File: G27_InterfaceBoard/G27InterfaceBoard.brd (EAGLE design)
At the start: 60 x 60 mm, 32 parts, among them IC1 LMV321M5, IC2 74HC126D, J1 Pedal, J2 Shifter, U1 LMV324

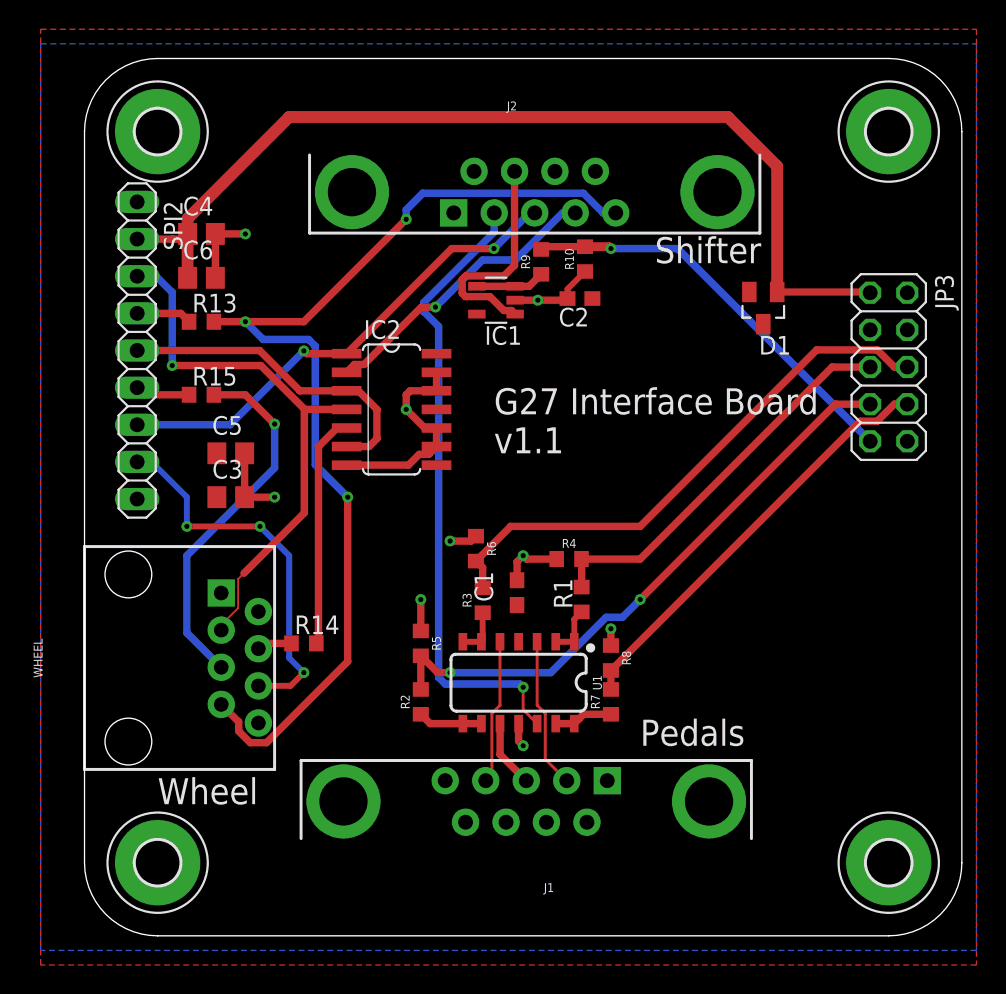
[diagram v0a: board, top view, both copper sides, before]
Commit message: Closer on G27 Interface v1.1:
Use buffer to boost 3.3V signals from STM32 to 5V logic to buy
better noise margin.
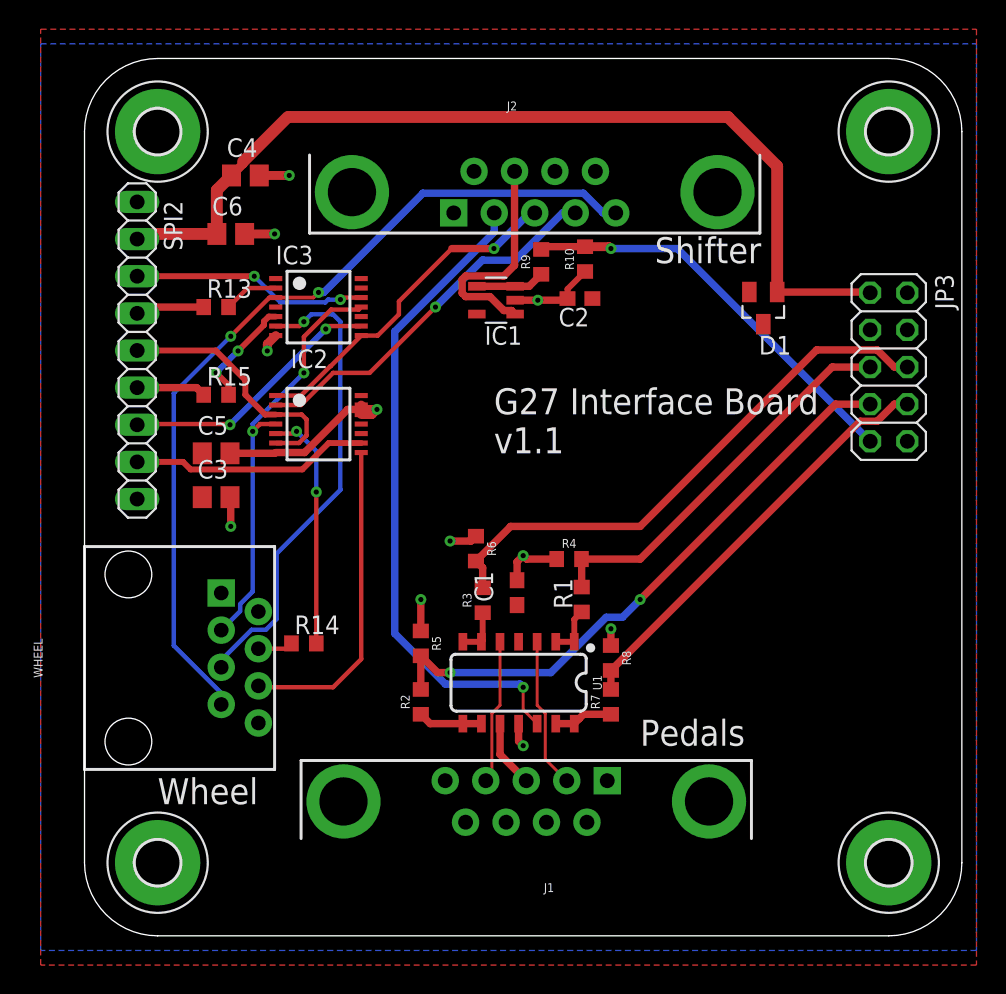
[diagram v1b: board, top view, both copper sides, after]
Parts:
- added IC3: 74AHCT126PW, 74xx-eu:TSSOP14
- IC2: value 74HC126D -> 74AHCT126PW; device 74xx-eu:SO14 -> 74xx-eu:TSSOP14
- R1, R2, R3, R7, R9: value 1.2k -> 1.5k
- moved IC2 5.10 mm to (16.0, -25.0)
- moved C4 5.00 mm to (11.0, -8.00)
- moved C6 3.61 mm to (10.0, -12.0)
- moved R13 1.41 mm to (9.00, -17.0)
- moved C3 1.00 mm to (9.00, -30.0)
- moved C5 1.00 mm to (9.00, -27.0)
- moved R15 1.00 mm to (9.00, -23.0)
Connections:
- new net MOSI_3V3: IC3.5, R15.2
- new net SCK_3V3: IC3.2, R13.2
- new net SHIFT_CS_3V3: IC3.9, SPI2.7
- new net WBTN_CS_3V3: IC3.12, SPI2.3
- new net WLED_LATCH_3V3: IC2.9, SPI2.8
- net GND: now also IC3.7; no longer IC2.10, IC2.9
- net MOSI: now also IC3.6; no longer R15.2
- net SCK: now also IC3.3; no longer R13.2
- net SHIFT_CS: now also IC3.8; no longer SPI2.7
- net VCC: now also IC2.10, IC3.1, IC3.10, IC3.13, IC3.14, IC3.4
- net WBTN_CS: now also IC3.11; no longer SPI2.3
- net WLED_LATCH: now also IC2.8; no longer SPI2.8
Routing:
- net SHIFT_CS_3V3: track 0.00 -> 18.3 mm, vias 0 -> 2
- net WLED_LATCH_3V3: track 0.00 -> 16.3 mm
- net WBTN_CS_3V3: track 0.00 -> 16.2 mm, vias 0 -> 2
- net SCK: track 72.4 -> 59.1 mm, vias 3 -> 2
- net SHIFT_CS: track 33.3 -> 23.4 mm, vias 2 -> 1
- net WBTN_CS: track 38.6 -> 29.0 mm, vias 1 -> 2
- net MOSI_3V3: track 0.00 -> 7.67 mm, vias 0 -> 2
- net MOSI: track 25.1 -> 32.5 mm
- net SHIFT_MISO: track 20.1 -> 25.9 mm
- net +3V3: track 70.9 -> 65.4 mm
- net MISO: track 22.4 -> 17.5 mm
- net GND: track 42.2 -> 37.4 mm, vias 9 -> 11
- net WLED_LATCH: track 26.3 -> 22.0 mm, vias 3 -> 0
- net SCK_3V3: track 0.00 -> 3.76 mm
- net SHIFT_X: track 43.1 -> 44.8 mm
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
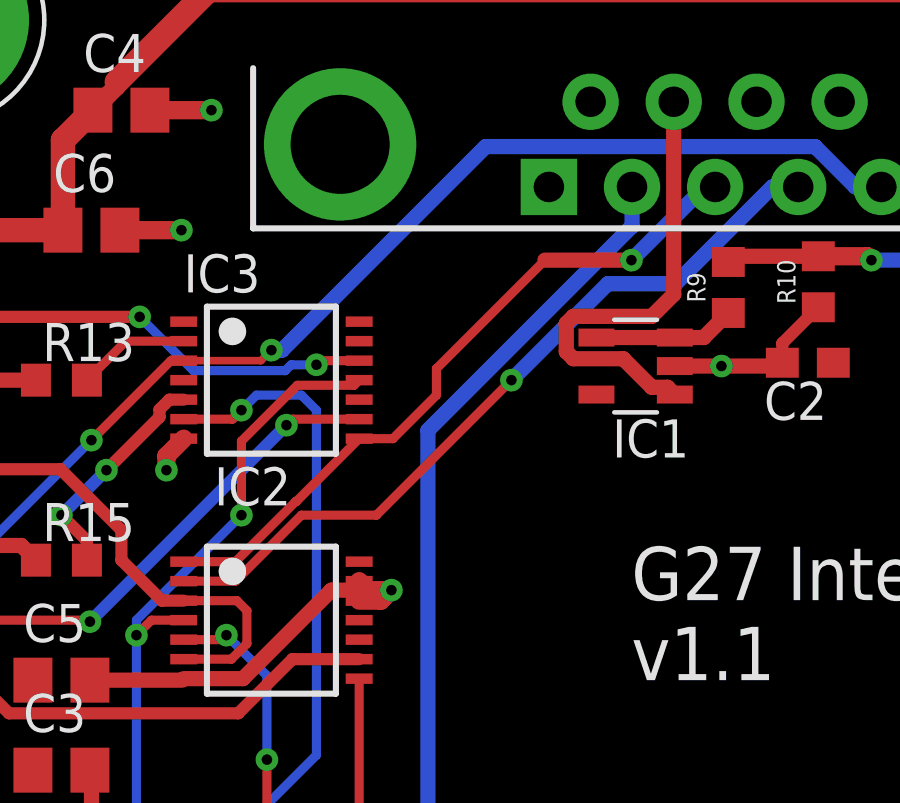
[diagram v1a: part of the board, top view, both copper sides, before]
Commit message: Add additional filter caps.
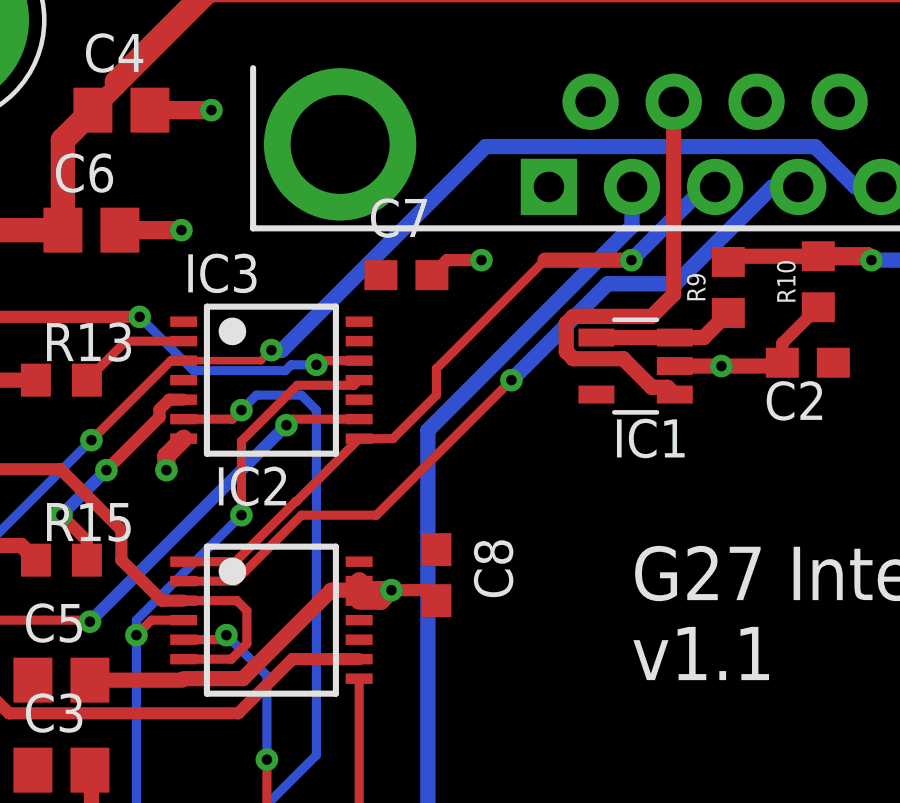
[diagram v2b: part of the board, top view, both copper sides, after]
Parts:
- added C7, C8: 0.1uF, resistor:C0603
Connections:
- net GND: now also C7.2, C8.2
- net VCC: now also C7.1, C8.1
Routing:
- net GND: track 37.4 -> 40.9 mm, vias 11 -> 12
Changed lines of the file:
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@@
 <attribute name="NAME" x="13.075" y="-14.075" size="1.27" layer="25"/>
+</element>
+<element name="C7" library="resistor" library_urn="urn:adsk.eagle:library:348" package="C0603" package3d_urn="urn:adsk.eagle:package:23616/2" value="0.1uF" x="20.5" y="-13.5" smashed="yes">
+<attribute name="NAME" x="19.23" y="-12.23" size="1.27" layer="25"/>
+<attribute name="VALUE" x="19.23" y="-16.04" size="1.27" layer="27"/>
+</element>
+<element name="C8" library="resistor" library_urn="urn:adsk.eagle:library:348" package="C0603" package3d_urn="urn:adsk.eagle:package:23616/2" value="0.1uF" x="21.5" y="-23.5" smashed="yes" rot="R270">
+<attribute name="NAME" x="22.77" y="-22.23" size="1.27" layer="25" rot="R270"/>
+<attribute name="VALUE" x="18.96" y="-22.23" size="1.27" layer="27" rot="R270"/>
 </element>
 </elements>
@@
 <wire x1="10" y1="-30.05" x2="10" y2="-32" width="0.508" layer="1"/>
 <via x="10" y="-32" extent="1-16" drill="0.35"/>
+<contactref element="C7" pad="2"/>
+<contactref element="C8" pad="2"/>
+<wire x1="21.5" y1="-24.35" x2="21.15" y2="-24" width="0.4064" layer="1"/>
+<wire x1="21.15" y1="-24" x2="20" y2="-24" width="0.4064" layer="1"/>
+<wire x1="21.35" y1="-13.5" x2="21.85" y2="-13" width="0.4064" layer="1"/>
+<wire x1="21.85" y1="-13" x2="23" y2="-13" width="0.4064" layer="1"/>
+<via x="23" y="-13" extent="1-16" drill="0.35"/>
 </signal>
 <signal name="SCK">
@@
 <contactref element="IC3" pad="10"/>
 <contactref element="IC3" pad="13"/>
+<contactref element="C7" pad="1"/>
+<contactref element="C8" pad="1"/>
 </signal>
 <signal name="WMISO">

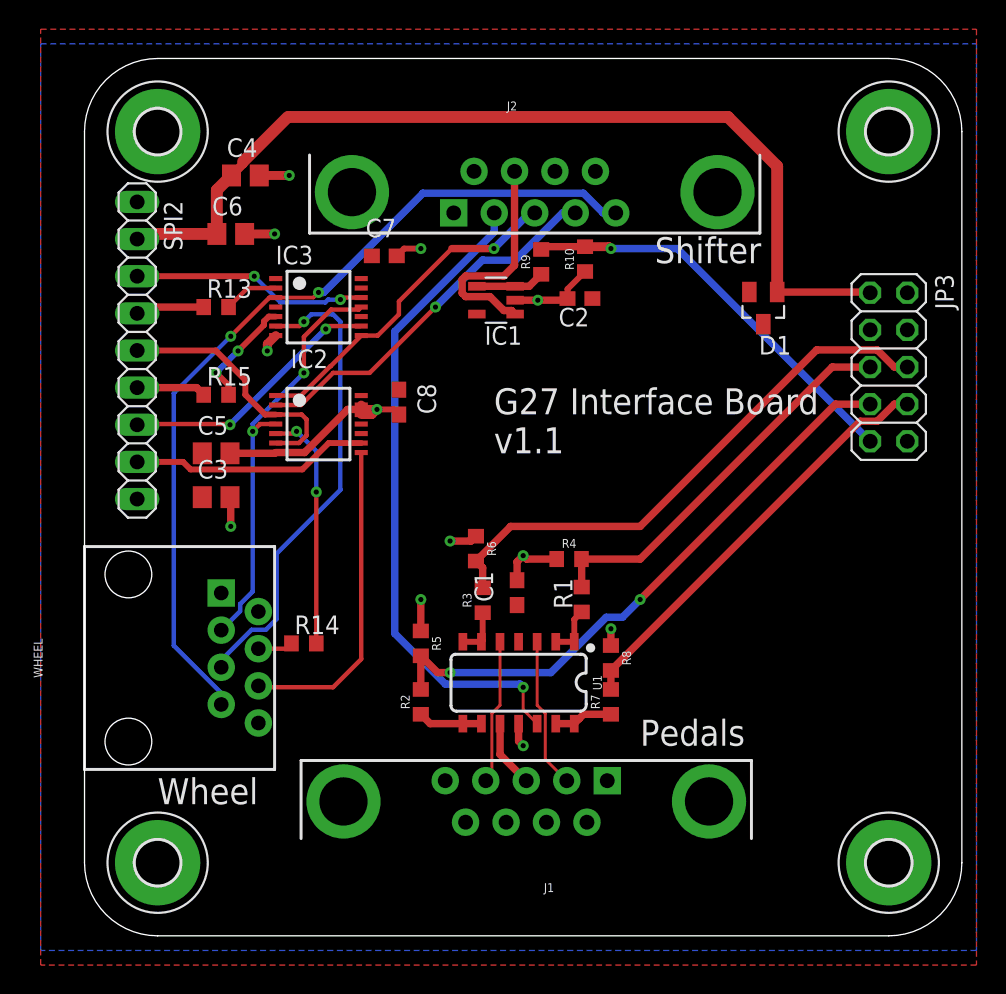
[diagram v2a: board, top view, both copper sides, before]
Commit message: Add voltage clamps to signals that could go above 3.3V.
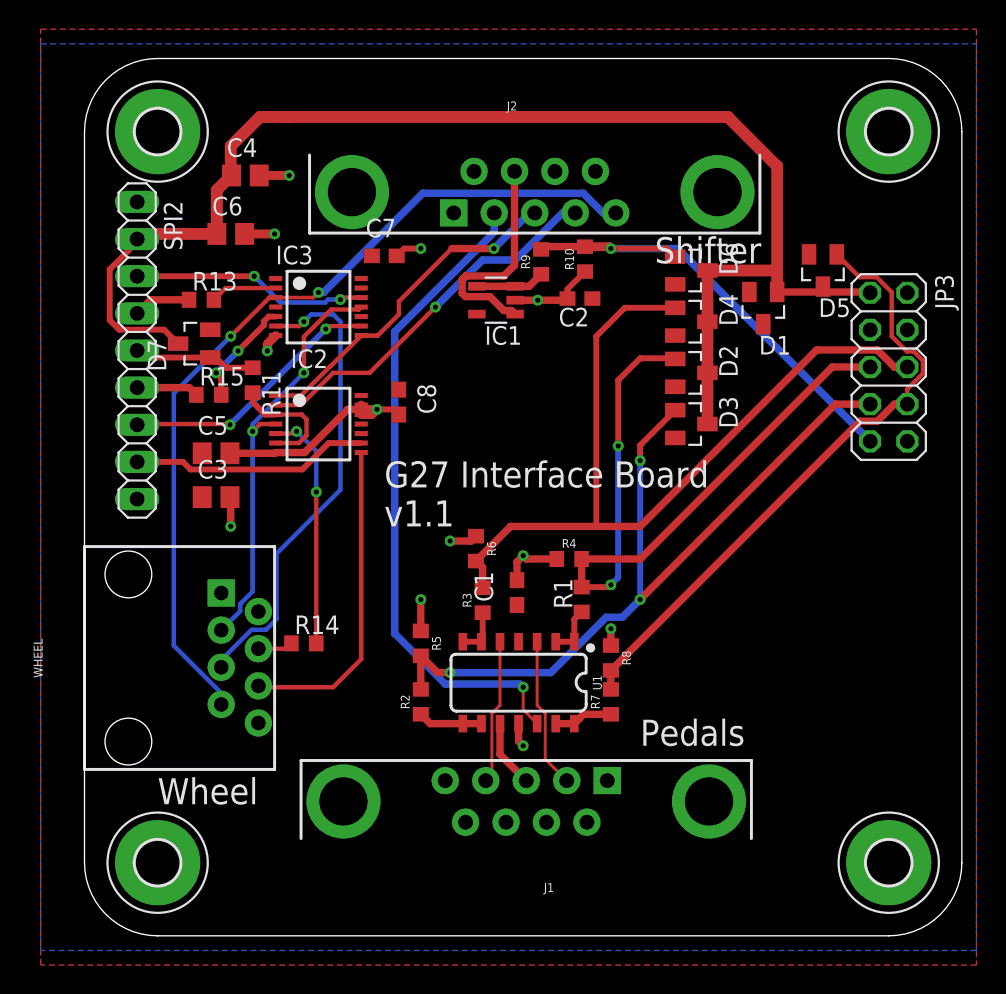
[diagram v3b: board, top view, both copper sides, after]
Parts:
- added D2, D3, D4, D5, D6, D7: BAT54, diode:SOT23
- added R11: 5k, resistor:R0603
- R1, R2, R3, R7, R9: value 1.5k -> 1.2k
- moved R13 1.12 mm to (8.00, -16.5)
- moved R15 0.50 mm to (8.50, -23.0)
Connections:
- new net N$4: D7.1, R11.1, SPI2.5
- net +3V3: now also D2.3, D3.3, D4.3, D5.3, D6.3, D7.3
- net BRAKE_3_3: now also D3.1
- net CLUTCH_3_3: now also D4.1
- net MISO: now also R11.2; no longer SPI2.5
- net SHIFT_X_3_3: now also D5.1
- net SHIFT_Y_3_3: now also D6.1
- net THROTTLE_3_3: now also D2.1
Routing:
- net +3V3: track 65.4 -> 93.9 mm
- net THROTTLE_3_3: track 27.1 -> 47.9 mm, vias 0 -> 2
- net CLUTCH_3_3: track 38.0 -> 57.2 mm
- net SHIFT_X_3_3: track 29.1 -> 43.2 mm
- net BRAKE_3_3: track 41.1 -> 55.1 mm, vias 2 -> 3
- net MISO: track 17.5 -> 8.25 mm
- net N$4: track 0.00 -> 8.39 mm
- net SHIFT_Y_3_3: track 28.1 -> 32.7 mm
- net SCK_3V3: track 3.76 -> 4.56 mm
- net N$8: track 4.73 -> 3.94 mm
- net N$10: track 4.75 -> 4.25 mm

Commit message: Add better 5V, 3.3V, and GND connections.
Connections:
- net +3V3: now also JP3.2
- net GND: now also JP3.3, JP3.4
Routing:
- net +3V3: track 93.9 -> 96.5 mm
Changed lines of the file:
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@@
 <wire x1="21.85" y1="-13" x2="23" y2="-13" width="0.4064" layer="1"/>
 <via x="23" y="-13" extent="1-16" drill="0.35"/>
+<contactref element="JP3" pad="4"/>
+<contactref element="JP3" pad="3"/>
 </signal>
 <signal name="SCK">
@@
 <contactref element="SPI2" pad="2"/>
 <wire x1="53.73" y1="-16.02" x2="53.68" y2="-15.97" width="0.508" layer="1"/>
-<wire x1="53.68" y1="-15.97" x2="50.5" y2="-15.97" width="0.508" layer="1"/>
-<wire x1="50.5" y1="-15.97" x2="47.37" y2="-15.97" width="0.508" layer="1"/>
-<wire x1="44" y1="-4" x2="14" y2="-4" width="0.8128" layer="1"/>
+<wire x1="53.68" y1="-15.97" x2="50.5" y2="-15.97" width="0.8128" layer="1"/>
+<wire x1="50.5" y1="-15.97" x2="47.37" y2="-15.97" width="0.8128" layer="1"/>
+<wire x1="44" y1="-4" x2="12" y2="-4" width="0.8128" layer="1"/>
 <wire x1="47.37" y1="-7.37" x2="47.37" y2="-14.5" width="0.8128" layer="1"/>
 <wire x1="47.37" y1="-14.5" x2="47.37" y2="-15.97" width="0.8128" layer="1"/>
@@
 <wire x1="1.7204" y1="-14.42706875" x2="3.6" y2="-12.54746875" width="0.4064" layer="1"/>
 <wire x1="1.7204" y1="-17.89293125" x2="1.7204" y2="-14.42706875" width="0.4064" layer="1"/>
-<wire x1="14" y1="-4" x2="12" y2="-4" width="0.8128" layer="1"/>
 <wire x1="12" y1="-4" x2="10" y2="-6" width="0.8128" layer="1"/>
 <wire x1="10" y1="-6" x2="10" y2="-7.95" width="0.8128" layer="1"/>
 <wire x1="10" y1="-7.95" x2="10.05" y2="-8" width="0.8128" layer="1"/>
+<contactref element="JP3" pad="2"/>
+<wire x1="56.27" y1="-16.02" x2="53.73" y2="-16.02" width="0.8128" layer="16"/>
 </signal>
 <signal name="WLED_LATCH">
@@
 <contactref element="C7" pad="1"/>
 <contactref element="C8" pad="1"/>
+<polygon width="0.15" layer="1" thermals="no">
+<vertex x="1.5" y="-29"/>
+<vertex x="1.5" y="-32"/>
+<vertex x="5.5" y="-32"/>
+<vertex x="5.5" y="-29"/>
+</polygon>
 </signal>
 <signal name="WMISO">

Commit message: Connect shift power LED to ground.
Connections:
- removed net !SHIFT_PWR_LED: J2.5
- net GND: now also J2.5
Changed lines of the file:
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@@
 <contactref element="JP3" pad="4"/>
 <contactref element="JP3" pad="3"/>
+<contactref element="J2" pad="5"/>
 </signal>
 <signal name="SCK">
@@
 <wire x1="39.85" y1="-13" x2="40.4" y2="-13.55" width="0.4064" layer="1"/>
 </signal>
-<signal name="!SHIFT_PWR_LED">
-<contactref element="J2" pad="5"/>
-</signal>
 <signal name="VCC">
